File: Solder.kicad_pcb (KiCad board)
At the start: 2 copper layers, 135.9 x 275.4 mm, 7 parts

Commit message: Finished? :D
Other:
- board text added: "My first PCB! Made for"
- board text removed: "Made for Hack Club's"
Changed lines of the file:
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@@
 	(net 0 "")
 	(net 1 "Net-(BT1--)")
-	(net 2 "GND")
-	(net 3 "Net-(D1-K)")
-	(net 4 "Net-(D2-K)")
+	(net 2 "Net-(D1-K)")
+	(net 3 "Net-(D2-K)")
+	(net 4 "GND")
 	(footprint "LED_THT:LED_D5.0mm"
 		(layer "F.Cu")
@@
 			(layers "*.Cu" "*.Mask")
 			(remove_unused_layers no)
-			(net 4 "Net-(D2-K)")
+			(net 3 "Net-(D2-K)")
 			(pinfunction "K")
 			(pintype "passive")
@@
 			(layers "*.Cu" "*.Mask")
 			(remove_unused_layers no)
-			(net 2 "GND")
+			(net 4 "GND")
 			(pinfunction "A")
 			(pintype "passive")
@@
 			(layers "*.Cu" "*.Mask")
 			(remove_unused_layers no)
-			(net 3 "Net-(D1-K)")
+			(net 2 "Net-(D1-K)")
 			(pintype "passive")
 		)
@@
 			(layers "*.Cu" "*.Mask")
 			(remove_unused_layers no)
-			(net 3 "Net-(D1-K)")
+			(net 2 "Net-(D1-K)")
 			(pinfunction "K")
 			(pintype "passive")
@@
 			(layers "*.Cu" "*.Mask")
 			(remove_unused_layers no)
-			(net 2 "GND")
+			(net 4 "GND")
 			(pinfunction "A")
 			(pintype "passive")
@@
 			(layers "*.Cu" "*.Mask")
 			(remove_unused_layers no)
-			(net 4 "Net-(D2-K)")
+			(net 3 "Net-(D2-K)")
 			(pintype "passive")
 		)
@@
 			(size 1.27 5.08)
 			(layers "F.Cu" "F.Mask" "F.Paste")
-			(net 2 "GND")
+			(net 4 "GND")
 			(pinfunction "+")
 			(pintype "passive")
@@
 			(size 1.27 5.08)
 			(layers "F.Cu" "F.Mask" "F.Paste")
-			(net 2 "GND")
+			(net 4 "GND")
 			(pinfunction "+")
 			(pintype "passive")
@@
 		)
 	)
-	(gr_text "Made for Hack Club's"
-		(at 132.25 54.75 0)
+	(gr_text "My first PCB! Made for"
+		(at 132 54 0)
 		(layer "B.SilkS")
 		(effects
@@
 	)
 	(segment
-		(start 116 52.5)
-		(end 113.5 55)
+		(start 104 50.38)
+		(end 111.34 50.38)
 		(width 0.2)
 		(layer "F.Cu")
@@
 	)
 	(segment
-		(start 115.765 66.765)
-		(end 116 67)
+		(start 111.34 50.38)
+		(end 113.46 52.5)
 		(width 0.2)
-		(layer "B.Cu")
+		(layer "F.Cu")
 		(net 2)
 	)
 	(segment
-		(start 104 50.38)
-		(end 111.34 50.38)
+		(start 104 69.81)
+		(end 111.15 69.81)
 		(width 0.2)
 		(layer "F.Cu")
@@
 	)
 	(segment
-		(start 111.34 50.38)
-		(end 113.46 52.5)
+		(start 111.15 69.81)
+		(end 113.46 67.5)
 		(width 0.2)
 		(layer "F.Cu")
@@
 	)
 	(segment
-		(start 104 69.81)
-		(end 111.15 69.81)
+		(start 116 52.5)
+		(end 113.5 55)
 		(width 0.2)
 		(layer "F.Cu")
@@
 	)
 	(segment
-		(start 111.15 69.81)
-		(end 113.46 67.5)
+		(start 115.765 66.765)
+		(end 116 67)
 		(width 0.2)
-		(layer "F.Cu")
+		(layer "B.Cu")
 		(net 4)
 	)
 	(zone
-		(net 2)
+		(net 4)
 		(net_name "GND")
 		(layers "F.Cu" "B.Cu")

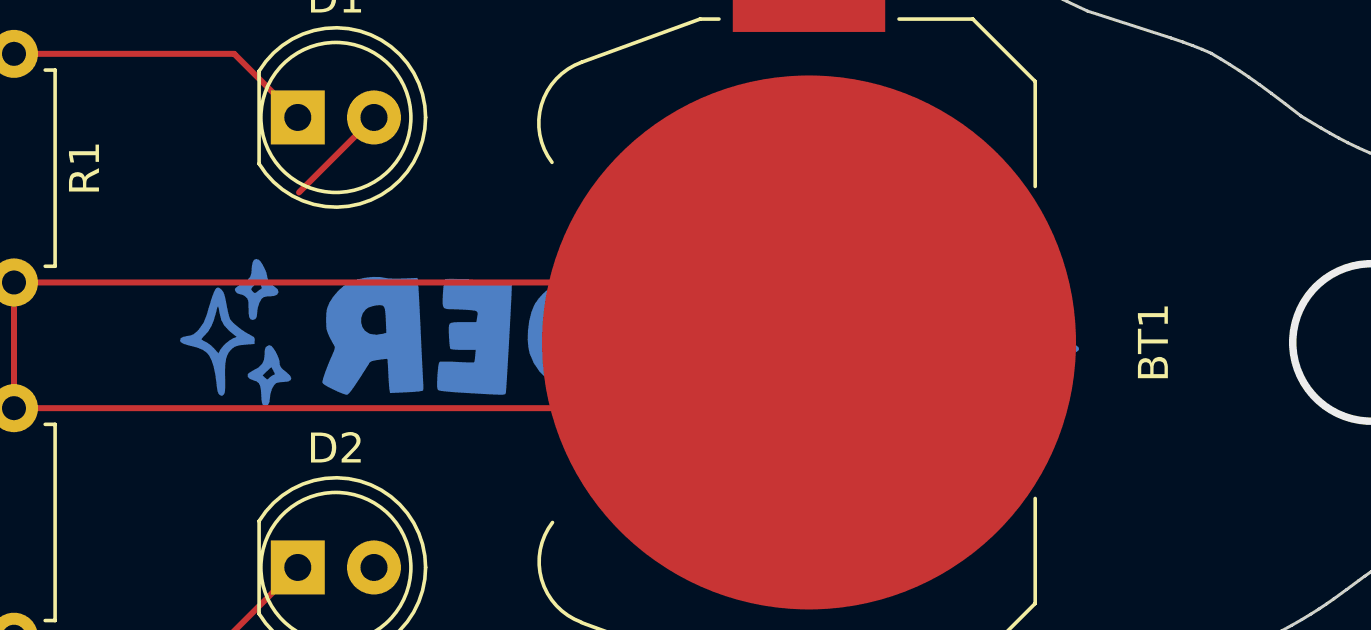
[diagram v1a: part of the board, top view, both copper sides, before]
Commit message: Moved text
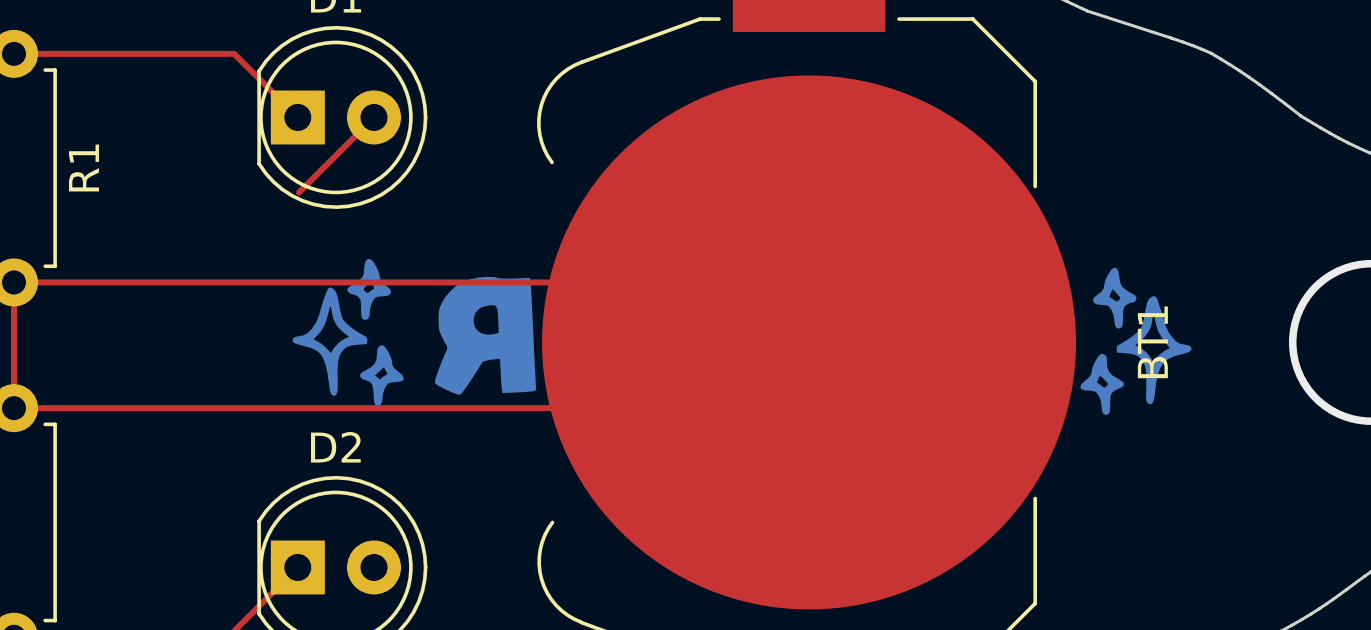
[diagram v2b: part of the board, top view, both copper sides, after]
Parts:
- moved G*** 3.75 mm to (128.2, 59.0)
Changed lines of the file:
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@@
 	(footprint "LOGO"
 		(layer "B.Cu")
-		(at 124.5 59 180)
+		(at 128.25 59 180)
 		(property "Reference" "G***"
 			(at 0 0 0)
@@
 	)
 	(gr_text "(You should join Hack Club)"
-		(at 134.25 66 0)
+		(at 139 65.25 0)
 		(layer "B.SilkS")
 		(effects
@@
 	)
 	(gr_text "My first PCB! Made for"
-		(at 132 54 0)
+		(at 135.75 54 0)
 		(layer "B.SilkS")
 		(effects

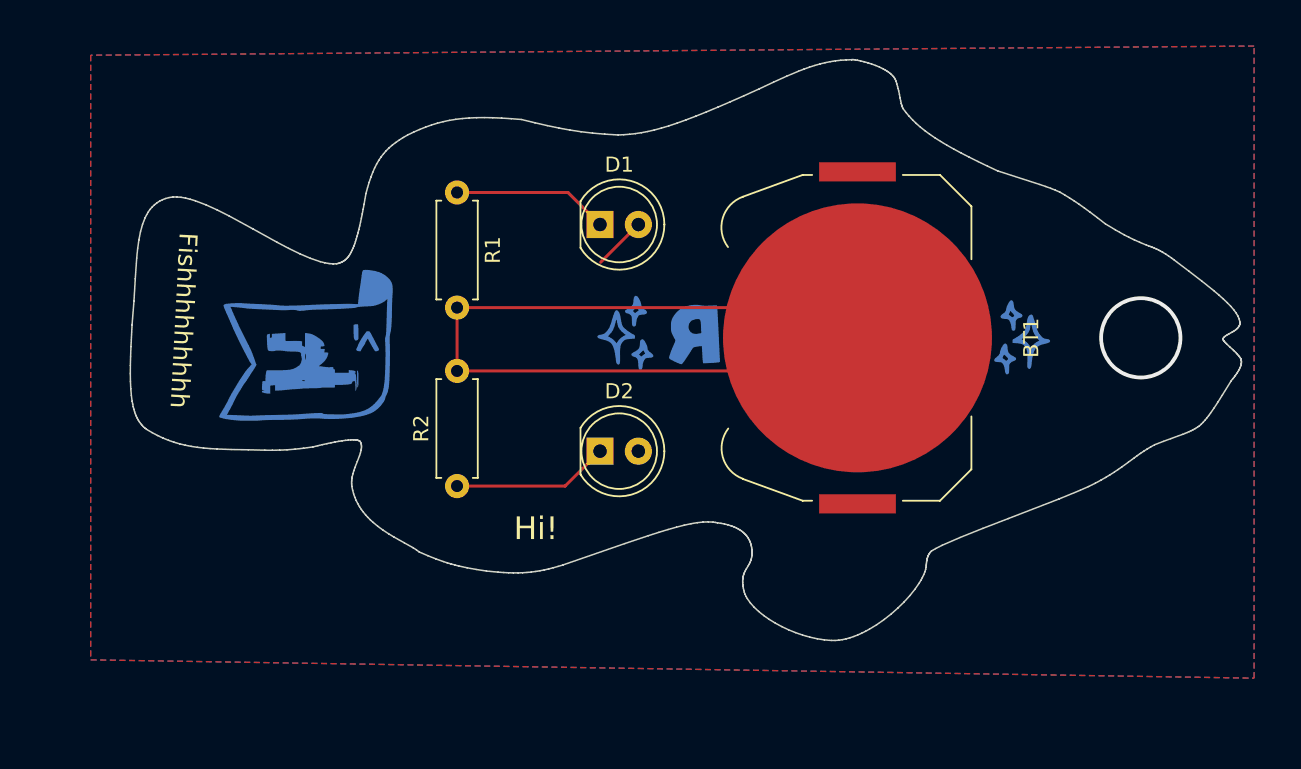
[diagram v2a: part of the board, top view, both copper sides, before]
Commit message: Add a button
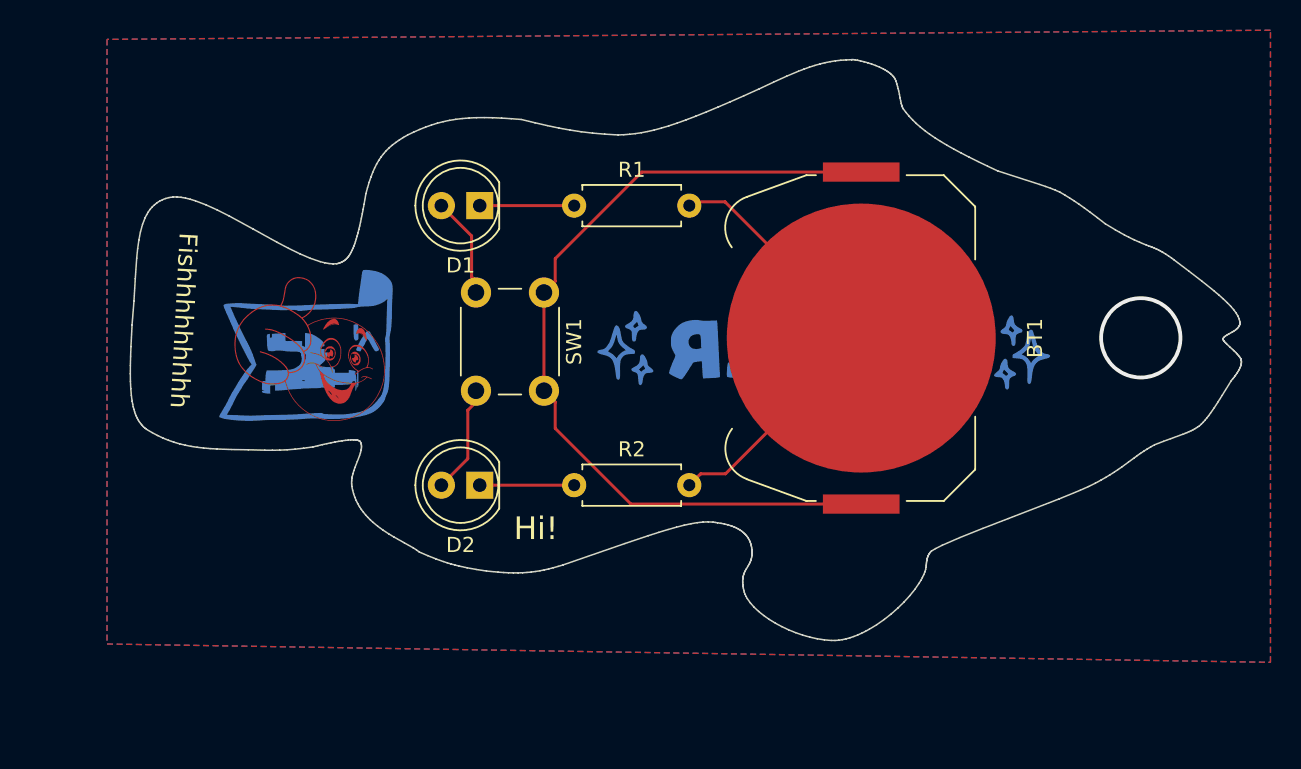
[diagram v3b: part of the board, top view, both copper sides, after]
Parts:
- added G***: LOGO, LOGO, F.Cu at (94.2, 60.8)
- added SW1: SW_Push, Button_Switch_THT:SW_PUSH_6mm, F.Cu at (109.8, 57.0)
- moved D2 8.27 mm to (105.5, 69.8), turned to 180 degrees
- moved D1 8.06 mm to (105.5, 51.2), turned to 180 degrees
- moved R1 7.80 mm to (111.8, 51.2), turned to 0 degrees
- moved R2 7.75 mm to (111.8, 69.8), turned to 0 degrees
- moved G*** 1.00 mm to (128.2, 60.0)
- moved BT1 0.25 mm to (130.8, 60.0)
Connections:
- BT1 pad 1: GND -> Net-(BT1-+)
- D1 pad 2: GND -> Net-(D1-A)
- D2 pad 2: GND -> Net-(D1-A)
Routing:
- net Net-(BT1-+): track 0.00 -> 56.8 mm
- net Net-(BT1--): track 58.9 -> 30.6 mm
- net Net-(D1-A): track 0.00 -> 14.7 mm
- net Net-(D2-K): track 10.4 -> 6.25 mm
- net Net-(D1-K): track 10.3 -> 6.25 mm
- net GND: track 3.87 -> 0.00 mm
- added copper zone on B.Cu, net Net-(D1-A)
- added copper zone on F.Cu, net Net-(D1-A)
- removed copper zone on B.Cu, net GND
- removed copper zone on F.Cu, net GND
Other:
- board text removed: "(Also, Hacklet is the BEST ysws!)"

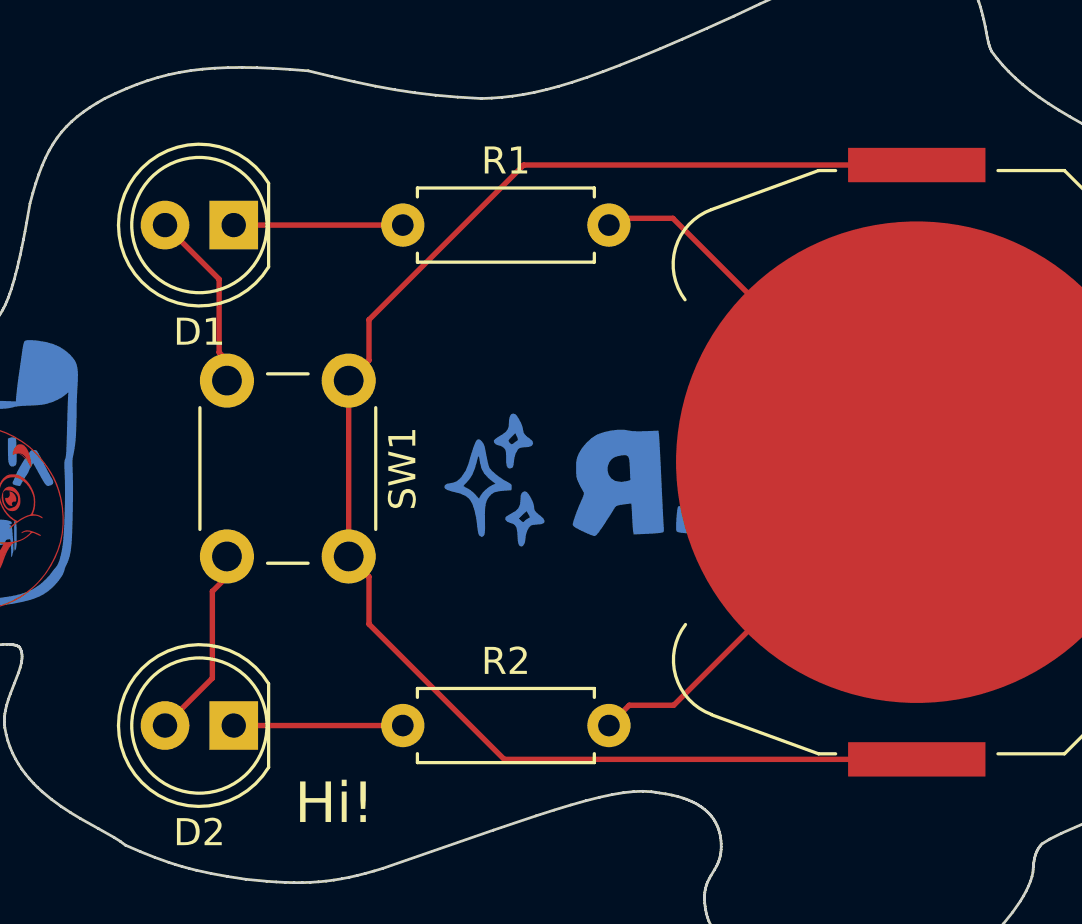
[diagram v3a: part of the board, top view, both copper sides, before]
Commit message: Fix ground fill
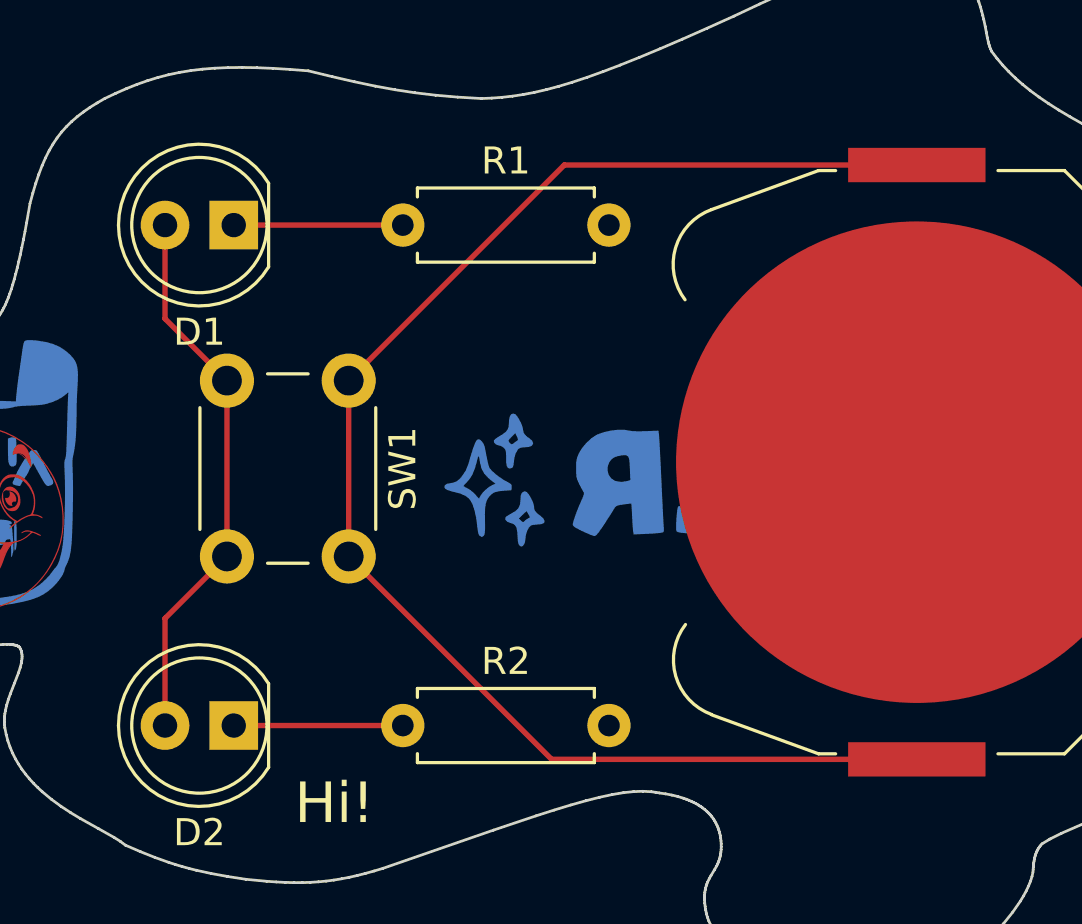
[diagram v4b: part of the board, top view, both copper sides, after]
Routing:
- net Net-(BT1--): track 30.6 -> 0.00 mm
- net Net-(D1-A): track 14.7 -> 21.2 mm
- net Net-(BT1-+): track 56.8 -> 54.9 mm
- added copper zone on B.Cu, net Net-(BT1--)
- added copper zone on F.Cu, net Net-(BT1--)
- removed copper zone on B.Cu, net Net-(D1-A)
- removed copper zone on F.Cu, net Net-(D1-A)
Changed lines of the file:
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@@
 	)
 	(segment
-		(start 121.735 51)
-		(end 130.75 60.015)
+		(start 117.72 49.03)
+		(end 130.75 49.03)
 		(width 0.2)
 		(layer "F.Cu")
-		(net 1)
+		(net 2)
 	)
 	(segment
-		(start 119.37 51.25)
-		(end 119.62 51)
+		(start 109.75 63.5)
+		(end 117.25 71)
 		(width 0.2)
 		(layer "F.Cu")
-		(net 1)
+		(net 2)
 	)
 	(segment
-		(start 121.765 69)
-		(end 130.75 60.015)
-		(width 0.2)
-		(layer "F.Cu")
-		(net 1)
-	)
-	(segment
-		(start 119.62 51)
-		(end 121.735 51)
-		(width 0.2)
-		(layer "F.Cu")
-		(net 1)
-	)
-	(segment
-		(start 119.37 69.75)
-		(end 120.12 69)
-		(width 0.2)
-		(layer "F.Cu")
-		(net 1)
-	)
-	(segment
-		(start 120.12 69)
-		(end 121.765 69)
-		(width 0.2)
-		(layer "F.Cu")
-		(net 1)
-	)
-	(segment
-		(start 115.5 71)
+		(start 117.25 71)
 		(end 130.75 71)
 		(width 0.2)
@@
 	(segment
 		(start 109.75 57)
-		(end 110.5 56.25)
-		(width 0.2)
-		(layer "F.Cu")
-		(net 2)
-	)
-	(segment
-		(start 110.5 56.25)
-		(end 110.5 54.75)
-		(width 0.2)
-		(layer "F.Cu")
-		(net 2)
-	)
-	(segment
-		(start 109.75 57)
-		(end 109.75 63.5)
-		(width 0.2)
-		(layer "F.Cu")
-		(net 2)
-	)
-	(segment
-		(start 110.5 64.25)
-		(end 110.5 66)
-		(width 0.2)
-		(layer "F.Cu")
-		(net 2)
-	)
-	(segment
-		(start 110.5 54.75)
-		(end 116.22 49.03)
-		(width 0.2)
-		(layer "F.Cu")
-		(net 2)
-	)
-	(segment
-		(start 110.5 66)
-		(end 115.5 71)
+		(end 117.72 49.03)
 		(width 0.2)
 		(layer "F.Cu")
@@
 	(segment
 		(start 109.75 63.5)
-		(end 110.5 64.25)
-		(width 0.2)
-		(layer "F.Cu")
-		(net 2)
-	)
-	(segment
-		(start 116.22 49.03)
-		(end 130.75 49.03)
+		(end 109.75 57)
 		(width 0.2)
 		(layer "F.Cu")
@@
 	)
 	(segment
-		(start 104.96 53.25)
-		(end 104.96 55.96)
+		(start 105.25 57)
+		(end 102.96 54.71)
 		(width 0.2)
 		(layer "F.Cu")
@@
 	)
 	(segment
-		(start 105.25 64.25)
-		(end 104.71 64.79)
+		(start 105.25 63.5)
+		(end 102.96 65.79)
 		(width 0.2)
 		(layer "F.Cu")
@@
 	)
 	(segment
-		(start 104.96 55.96)
-		(end 105.25 56.25)
+		(start 105.25 57)
+		(end 105.25 63.5)
 		(width 0.2)
 		(layer "F.Cu")
@@
 	)
 	(segment
-		(start 104.71 68)
+		(start 102.96 65.79)
 		(end 102.96 69.75)
-		(width 0.2)
-		(layer "F.Cu")
-		(net 5)
-	)
-	(segment
-		(start 104.71 64.79)
-		(end 104.71 68)
-		(width 0.2)
-		(layer "F.Cu")
-		(net 5)
-	)
-	(segment
-		(start 105.25 56.25)
-		(end 105.25 57)
 		(width 0.2)
 		(layer "F.Cu")
@@
 	)
 	(segment
-		(start 105.25 63.5)
-		(end 105.25 64.25)
-		(width 0.2)
-		(layer "F.Cu")
-		(net 5)
-	)
-	(segment
-		(start 102.96 51.25)
-		(end 104.96 53.25)
+		(start 102.96 54.71)
+		(end 102.96 51.25)
 		(width 0.2)
 		(layer "F.Cu")
@@
 	)
 	(zone
-		(net 5)
-		(net_name "Net-(D1-A)")
+		(net 1)
+		(net_name "Net-(BT1--)")
 		(layers "F.Cu" "B.Cu")
 		(hatch edge 0.5)
